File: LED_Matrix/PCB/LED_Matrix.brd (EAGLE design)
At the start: 32 x 32 mm, 8 parts, among them U1 ATTINY48, U2 ULN2803AFWG

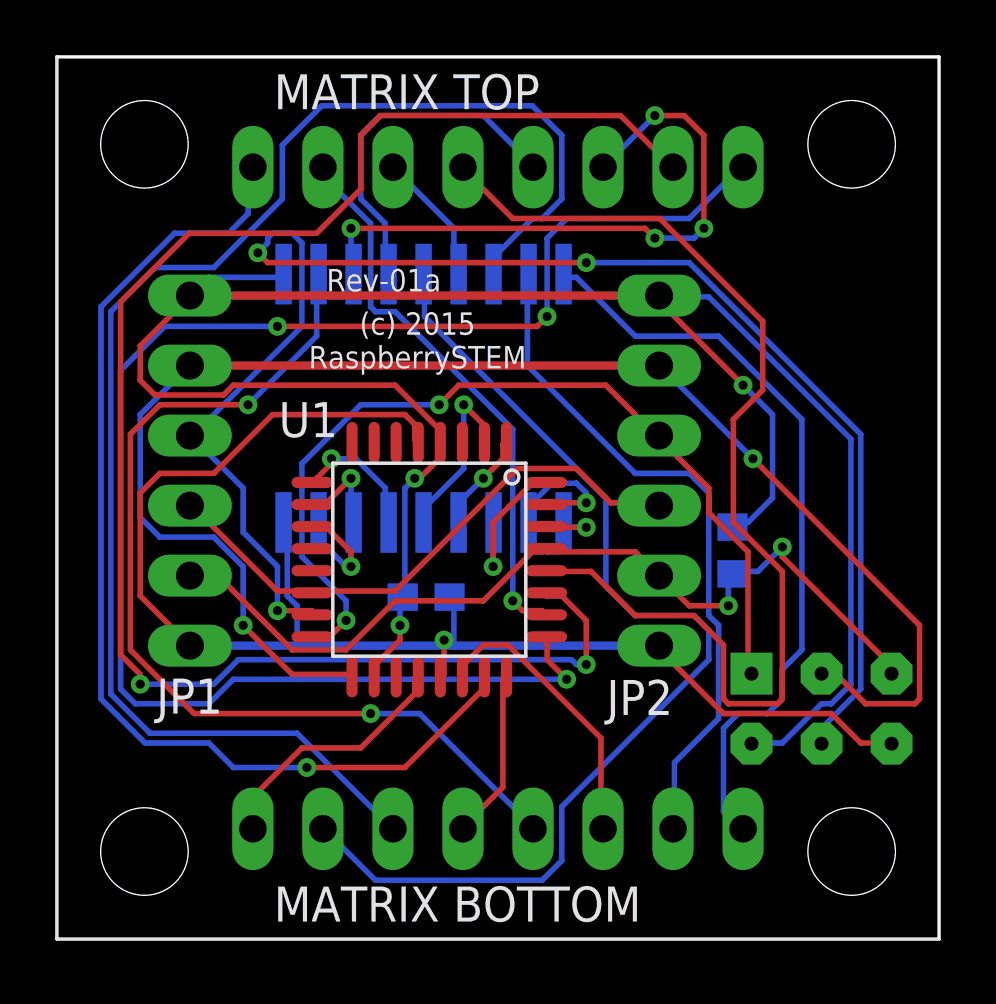
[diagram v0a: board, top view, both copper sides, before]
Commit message: matrix - Rev-01b - Adjust size, mouting holes, split matrix connector.  No routing changes.
Dimensionsional, mounting, silkscreen and schematic changes.  (actually - there
was one very minor routing adjustment where a DRC check failed).

Changes:
    - Board was 1260x1260mils: changed to correct 1250x1250, which is the size
      of the LED matrix.
    - Mouting holes where 1010 mils apart, and still would hit the matrix
      headers with #4 screws.  Rather than do the correct 1000mils, went to
      1050 mils, which allow us only of one pair of mounting pins at a time.
      This is good because it allows all boards in a chain to use exactly two
      mounting holes.  Holes are now also labeled on the silkscreen.
    - Split LED matrix connector so that the BOM can have correct reference
      designator linkages.
    - Changed JP1/2 to more correct J/P designations
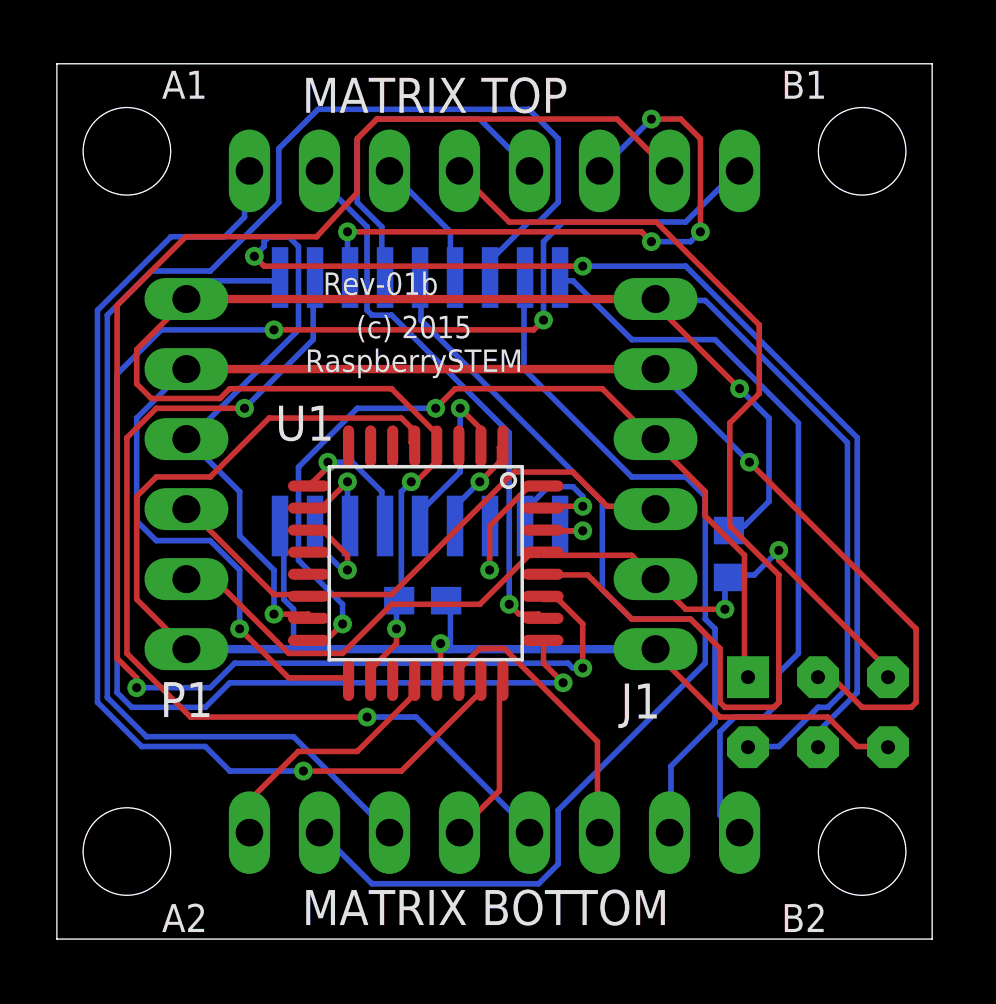
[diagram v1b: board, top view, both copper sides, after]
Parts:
- removed JP1, JP2: NONE, LED_Matrix:1X06
- removed LEDMATRIX: 8X8_LED_MATRIX, LED_Matrix:8X8_LED_MATRIX
- added J1, P1: NONE, LED_Matrix:1X06
- added J2, J3: HEADER-1X8, LED_Matrix:HEADER-1X8
- moved C1 0.18 mm to (13.3, 12.3)
- moved PROG 0.18 mm to (27.6, 8.23)
- moved R1 0.18 mm to (24.4, 14.0)
- moved U2 0.18 mm to (18.3, 15.0)
- moved U1 0.18 mm to (13.4, 13.6)
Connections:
- removed net N$1: LEDMATRIX.COL0, U2.O1
- removed net N$2: LEDMATRIX.COL1, U2.O2
- removed net N$3: LEDMATRIX.COL2, U2.O3
- removed net N$4: LEDMATRIX.COL3, U2.O4
- removed net N$5: LEDMATRIX.COL4, U2.O5
- removed net N$6: LEDMATRIX.COL5, U2.O6
- removed net N$7: LEDMATRIX.COL6, U2.O7
- removed net N$8: LEDMATRIX.COL7, U2.O8
- new net COL0_SINK: U1.PD0, U2.I1
- new net COL1_SINK: U1.PD1, U2.I2
- new net COL2_SINK: U1.PD2, U2.I3
- new net COL3_SINK: U1.PD3, U2.I4
- new net COL4_SINK: U1.PD4, U2.I5
- new net COL5_SINK: U1.PD5, U2.I6
- new net COL6_SINK: U1.PD6, U2.I7
- new net COL7_SINK: U1.PD7, U2.I8
- net COL0: now also J3.8, U2.O1; no longer U1.PD0, U2.I1
- net COL1: now also J3.7, U2.O2; no longer U1.PD1, U2.I2
- net COL2: now also J3.3, U2.O3; no longer U1.PD2, U2.I3
- net COL3: now also J2.3, U2.O4; no longer U1.PD3, U2.I4
- net COL4: now also J3.2, U2.O5; no longer U1.PD4, U2.I5
- net COL5: now also J2.5, U2.O6; no longer U1.PD5, U2.I6
- net COL6: now also J2.6, U2.O7; no longer U1.PD6, U2.I7
- net COL7: now also J3.5, U2.O8; no longer U1.PD7, U2.I8
- net CS: now also J1.4, P1.4; no longer JP1.4, JP2.4
- net GND: now also J1.6, P1.6; no longer JP1.6, JP2.6
- net MISO: now also J1.3; no longer JP2.3
- net MOSI: now also P1.3; no longer JP1.3
- net RESET: now also J1.5, P1.5; no longer JP1.5, JP2.5
- net ROW0: now also J3.1; no longer LEDMATRIX.ROW0
- net ROW1: now also J3.6; no longer LEDMATRIX.ROW1
- net ROW2: now also J2.1; no longer LEDMATRIX.ROW2
- net ROW3: now also J3.4; no longer LEDMATRIX.ROW3
- net ROW4: now also J2.8; no longer LEDMATRIX.ROW4
- net ROW5: now also J2.2; no longer LEDMATRIX.ROW5
- net ROW6: now also J2.7; no longer LEDMATRIX.ROW6
- net ROW7: now also J2.4; no longer LEDMATRIX.ROW7
- net SCK: now also J1.2, P1.2; no longer JP1.2, JP2.2
- net VCC: now also J1.1, P1.1; no longer JP1.1, JP2.1
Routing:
- net N$3: track 53.5 -> 0.00 mm
- net COL2: track 5.72 -> 53.3 mm, vias 1 -> 0
- net N$5: track 38.7 -> 0.00 mm
- net N$8: track 35.6 -> 0.00 mm, vias 2 -> 0
- net COL4: track 6.56 -> 38.6 mm, vias 1 -> 0
- net COL7: track 4.49 -> 35.6 mm, vias 1 -> 2
- net N$1: track 27.8 -> 0.00 mm
- net COL0: track 2.37 -> 27.6 mm, vias 1 -> 0
- net N$2: track 24.8 -> 0.00 mm
- net N$7: track 22.9 -> 0.00 mm, vias 4 -> 0
- net COL1: track 5.09 -> 24.7 mm, vias 1 -> 0
- net COL6: track 3.48 -> 22.8 mm, vias 1 -> 4
- net N$6: track 12.8 -> 0.00 mm
- net COL5: track 4.92 -> 12.7 mm, vias 1 -> 0
- net COL4_SINK: track 0.00 -> 6.56 mm, vias 0 -> 1
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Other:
- board size 32 x 32 mm -> 31.8 x 31.8 mm
- board text added: "A1"
- board text added: "A2"
- board text added: "B1"
- board text added: "B2"
- board text added: "Rev-01b"
- board text removed: "Rev-01a"
